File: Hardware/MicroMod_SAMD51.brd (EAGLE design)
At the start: 22 x 22 mm, 36 parts, among them J2 MICROMOD-2222, U1 W25QXX128MBIT-6X5-NO_CENTER, U2 ATSAMD51J20A-A, Y1 32.768kHz

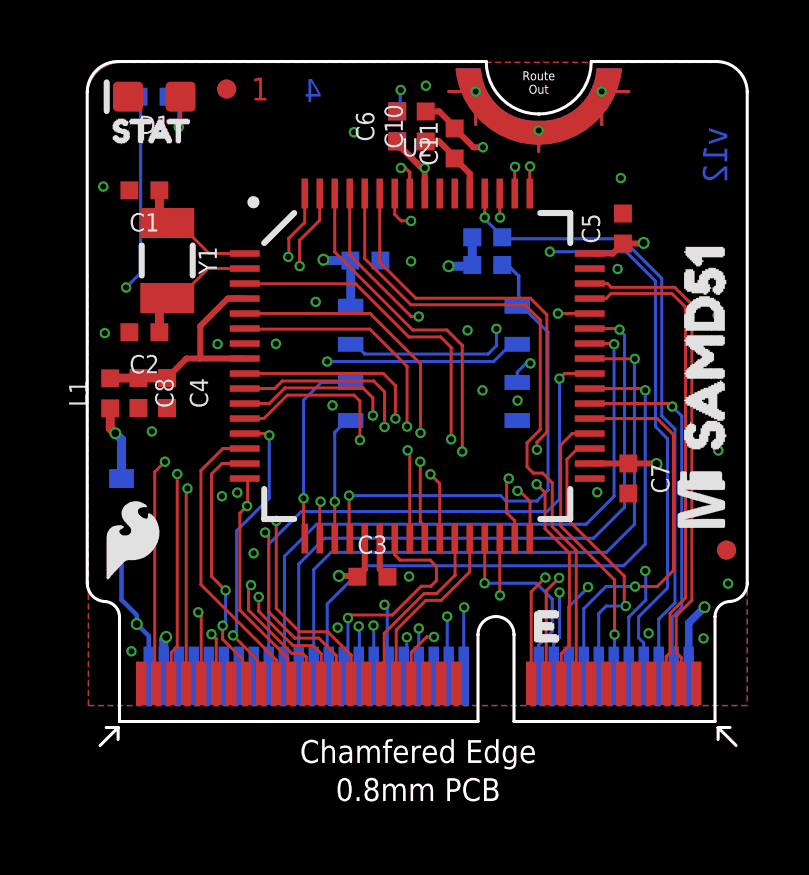
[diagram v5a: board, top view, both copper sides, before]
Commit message: fixes stray via
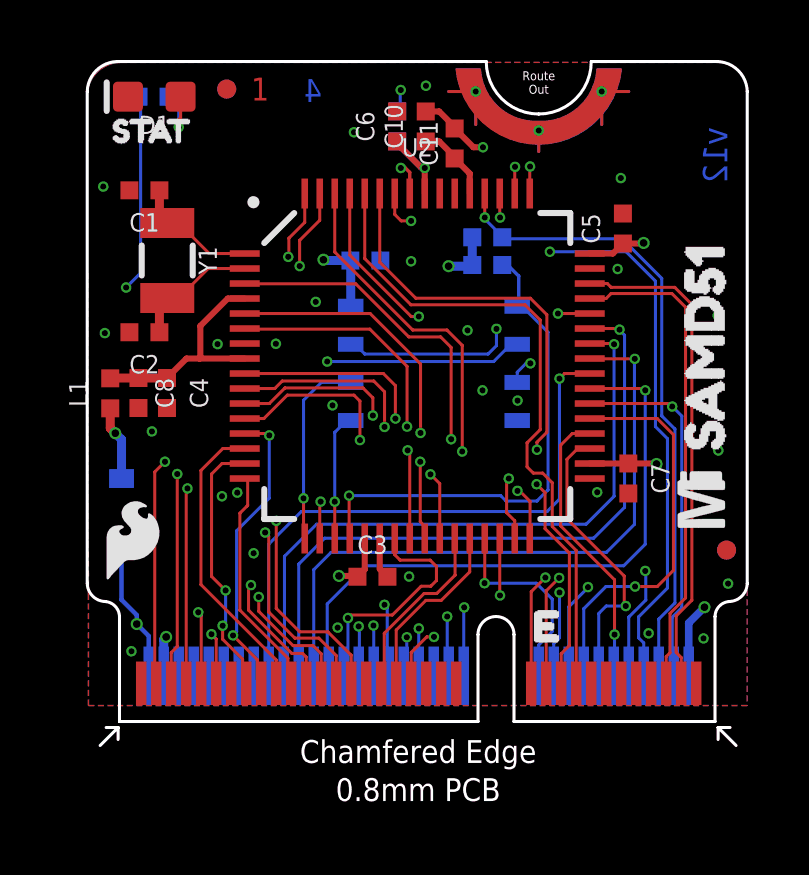
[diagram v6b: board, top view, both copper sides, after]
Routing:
- net !CS: vias 1 -> 0
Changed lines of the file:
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@@
 <setting verticaltext="up"/>
 </settings>
-<grid distance="0.5" unitdist="mm" unit="mm" style="dots" multiple="1" display="yes" altdistance="0.01" altunitdist="mm" altunit="mm"/>
+<grid distance="0.05" unitdist="inch" unit="inch" style="dots" multiple="1" display="yes" altdistance="0.005" altunitdist="inch" altunit="inch"/>
 <layers>
 <layer number="1" name="Top" color="4" fill="1" visible="yes" active="yes"/>
-<layer number="2" name="PWR_HORIZ" color="1" fill="3" visible="yes" active="yes"/>
-<layer number="15" name="GND-VERT" color="4" fill="6" visible="yes" active="yes"/>
+<layer number="2" name="PWR_HORIZ" color="1" fill="3" visible="no" active="yes"/>
+<layer number="15" name="GND-VERT" color="4" fill="6" visible="no" active="yes"/>
 <layer number="16" name="Bottom" color="3" fill="1" visible="yes" active="yes"/>
 <layer number="17" name="Pads" color="26" fill="1" visible="yes" active="yes"/>
@@
 <layer number="19" name="Unrouted" color="6" fill="1" visible="yes" active="yes"/>
 <layer number="20" name="Dimension" color="15" fill="1" visible="yes" active="yes"/>
-<layer number="21" name="tPlace" color="16" fill="1" visible="no" active="yes"/>
-<layer number="22" name="bPlace" color="14" fill="1" visible="no" active="yes"/>
+<layer number="21" name="tPlace" color="16" fill="1" visible="yes" active="yes"/>
+<layer number="22" name="bPlace" color="14" fill="1" visible="yes" active="yes"/>
 <layer number="23" name="tOrigins" color="15" fill="1" visible="yes" active="yes"/>
 <layer number="24" name="bOrigins" color="15" fill="1" visible="yes" active="yes"/>
@@
 </signal>
 <signal name="!CS">
-<via x="5.3278" y="7.1834" extent="1-16" drill="0.2"/>
 <contactref element="U2" pad="16"/>
 <wire x1="5.3478" y1="8.1" x2="5.3478" y2="7.2034" width="0.1016" layer="1"/>
